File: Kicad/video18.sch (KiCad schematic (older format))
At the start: 18 parts, among them J201 DE15HD, U201 THS7316, U202 TPD7S019

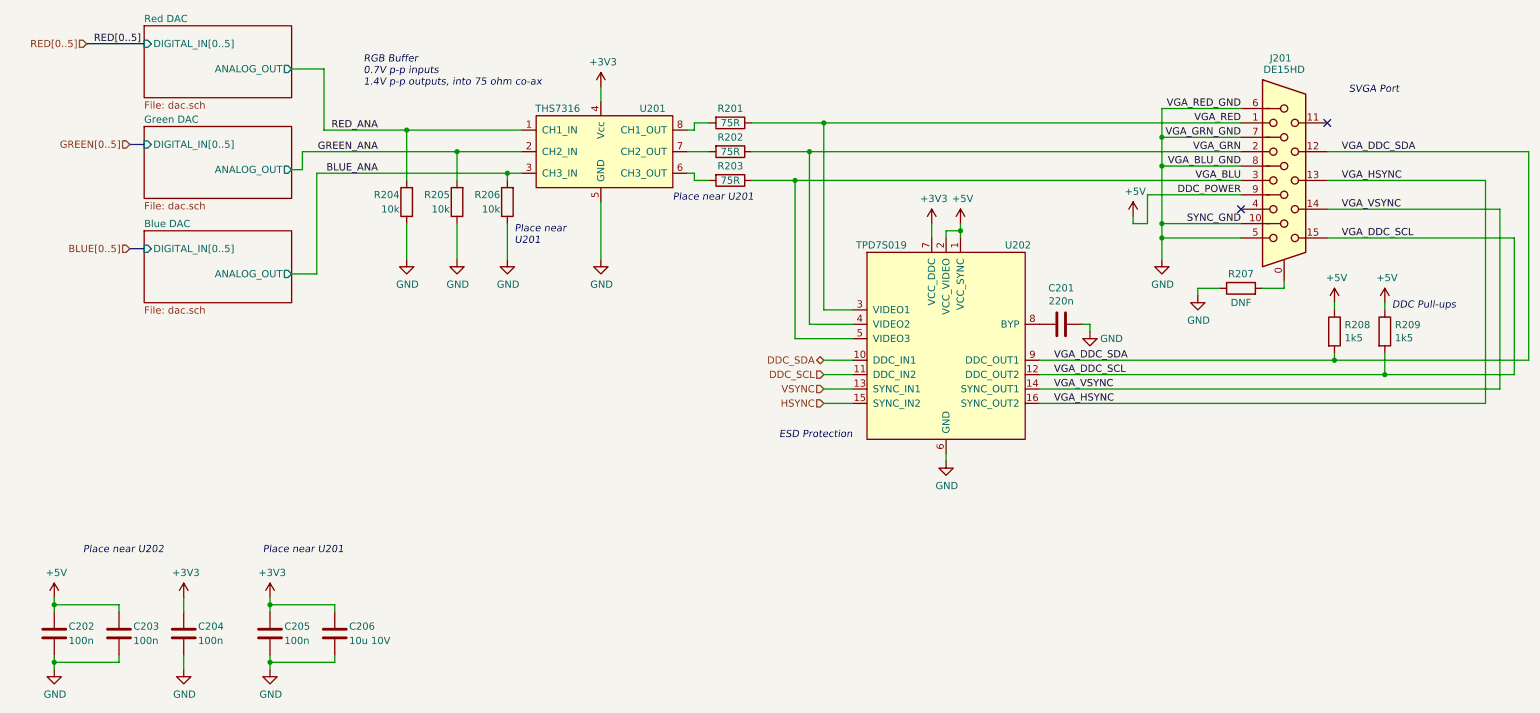
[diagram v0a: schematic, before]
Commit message: Added 12-bit video DAC.
Also had to change footprints to suit Kicad 5.1.9
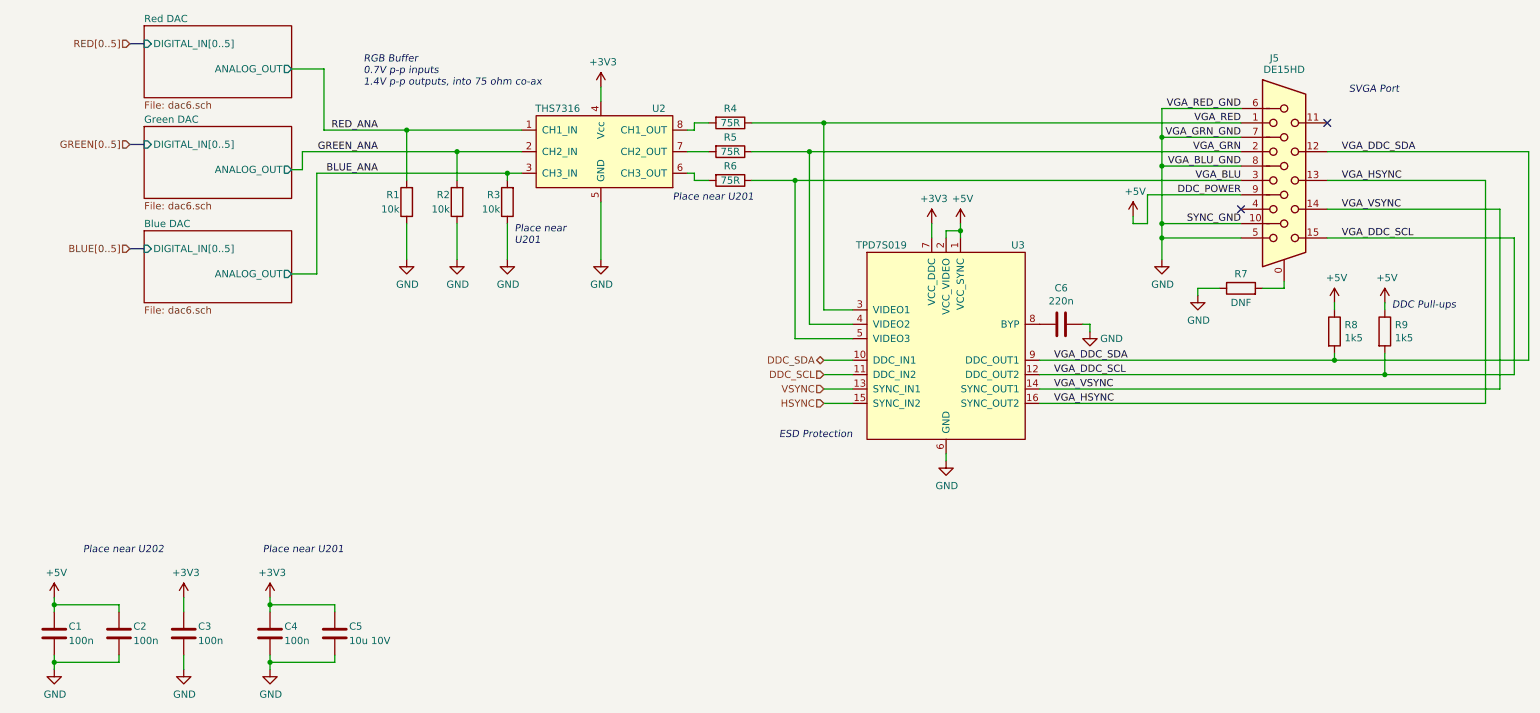
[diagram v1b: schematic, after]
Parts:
- removed C203, C205: 100n, Capacitor_SMD:C_0805_2012Metric_Pad1.15x1.40mm_HandSolder, symbol Device:C
- removed C206: 10u 10V, Capacitor_SMD:C_0805_2012Metric_Pad1.15x1.40mm_HandSolder, symbol Device:C
- removed R205, R206: 10k, Resistor_SMD:R_0805_2012Metric_Pad1.15x1.40mm_HandSolder, symbol Device:R
- removed R207: DNF, Resistor_SMD:R_0805_2012Metric_Pad1.15x1.40mm_HandSolder, symbol Device:R
- removed U201: THS7316, Package_SO:SOIC-8_3.9x4.9mm_P1.27mm, symbol Neotron-Common-Hardware:TPF133A
- removed U202: TPD7S019, Package_SO:SSOP-16_3.9x4.9mm_P0.635mm, symbol Neotron-Common-Hardware:TPD7S019
- added C2, C4: 100n, Capacitor_SMD:C_0805_2012Metric_Pad1.18x1.45mm_HandSolder, symbol Device:C
- added C5: 10u 10V, Capacitor_SMD:C_0805_2012Metric_Pad1.18x1.45mm_HandSolder, symbol Device:C
- added R2, R3: 10k, Resistor_SMD:R_0805_2012Metric_Pad1.20x1.40mm_HandSolder, symbol Device:R
- added R7: DNF, Resistor_SMD:R_0805_2012Metric_Pad1.20x1.40mm_HandSolder, symbol Device:R
- added U2: THS7316, Package_SO:SOIC-8_3.9x4.9mm_P1.27mm, symbol Neotron-Common-Hardware:TPF133A
- added U3: TPD7S019, Package_SO:SSOP-16_3.9x4.9mm_P0.635mm, symbol Neotron-Common-Hardware:TPD7S019
- C1: renamed from C202; footprint Capacitor_SMD:C_0805_2012Metric_Pad1.15x1.40mm_HandSolder -> Capacitor_SMD:C_0805_2012Metric_Pad1.18x1.45mm_HandSolder
- C3: renamed from C204; footprint Capacitor_SMD:C_0805_2012Metric_Pad1.15x1.40mm_HandSolder -> Capacitor_SMD:C_0805_2012Metric_Pad1.18x1.45mm_HandSolder
- C6: renamed from C201; footprint Capacitor_SMD:C_0805_2012Metric_Pad1.15x1.40mm_HandSolder -> Capacitor_SMD:C_0805_2012Metric_Pad1.18x1.45mm_HandSolder
- R1: renamed from R204; footprint Resistor_SMD:R_0805_2012Metric_Pad1.15x1.40mm_HandSolder -> Resistor_SMD:R_0805_2012Metric_Pad1.20x1.40mm_HandSolder
- R4: renamed from R201; footprint Resistor_SMD:R_0805_2012Metric_Pad1.15x1.40mm_HandSolder -> Resistor_SMD:R_0805_2012Metric_Pad1.20x1.40mm_HandSolder
- R5: renamed from R202; footprint Resistor_SMD:R_0805_2012Metric_Pad1.15x1.40mm_HandSolder -> Resistor_SMD:R_0805_2012Metric_Pad1.20x1.40mm_HandSolder
- R6: renamed from R203; footprint Resistor_SMD:R_0805_2012Metric_Pad1.15x1.40mm_HandSolder -> Resistor_SMD:R_0805_2012Metric_Pad1.20x1.40mm_HandSolder
- R8: renamed from R208; footprint Resistor_SMD:R_0805_2012Metric_Pad1.15x1.40mm_HandSolder -> Resistor_SMD:R_0805_2012Metric_Pad1.20x1.40mm_HandSolder
- R9: renamed from R209; footprint Resistor_SMD:R_0805_2012Metric_Pad1.15x1.40mm_HandSolder -> Resistor_SMD:R_0805_2012Metric_Pad1.20x1.40mm_HandSolder
- renumbered J201 to J5
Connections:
- net +3V3: now also C4.2, C5.1, U2.4 (Vcc), U3.7 (VCC_DDC)
- net +5V: now also C2.2, U3.1 (VCC_SYNC), U3.2 (VCC_VIDEO)
- net BLUE_ANA: now also R3.2, U2.3 (CH3_IN)
- net DDC_SCL: now also U3.11 (DDC_IN2)
- net DDC_SDA: now also U3.10 (DDC_IN1)
- net GND: now also C2.1, C4.1, C5.2, R2.1, R3.1, R7.1, U2.5 (GND), U3.6 (GND)
- net GREEN_ANA: now also R2.2, U2.2 (CH2_IN)
- net HSYNC: now also U3.15 (SYNC_IN2)
- net RED_ANA: now also U2.1 (CH1_IN)
- net VGA_BLU: now also U3.5 (VIDEO3)
- net VGA_DDC_SCL: now also U3.12 (DDC_OUT2)
- net VGA_DDC_SDA: now also U3.9 (DDC_OUT1)
- net VGA_GRN: now also U3.4 (VIDEO2)
- net VGA_HSYNC: now also U3.16 (SYNC_OUT2)
- net VGA_RED: now also U3.3 (VIDEO1)
- net VGA_VSYNC: now also U3.14 (SYNC_OUT1)
- net VSYNC: now also U3.13 (SYNC_IN1)
- net at J5.0: now also R7.2
- net at R4.2: now also U2.8 (CH1_OUT)
- net at R5.2: now also U2.7 (CH2_OUT)
- net at R6.2: now also U2.6 (CH3_OUT)
- net at C6.2: now also U3.8 (BYP)

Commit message: Add 4-bit Video DAC, and re-wire BMC.
Now the BMC is an SPI device, and has a four-wire UART.
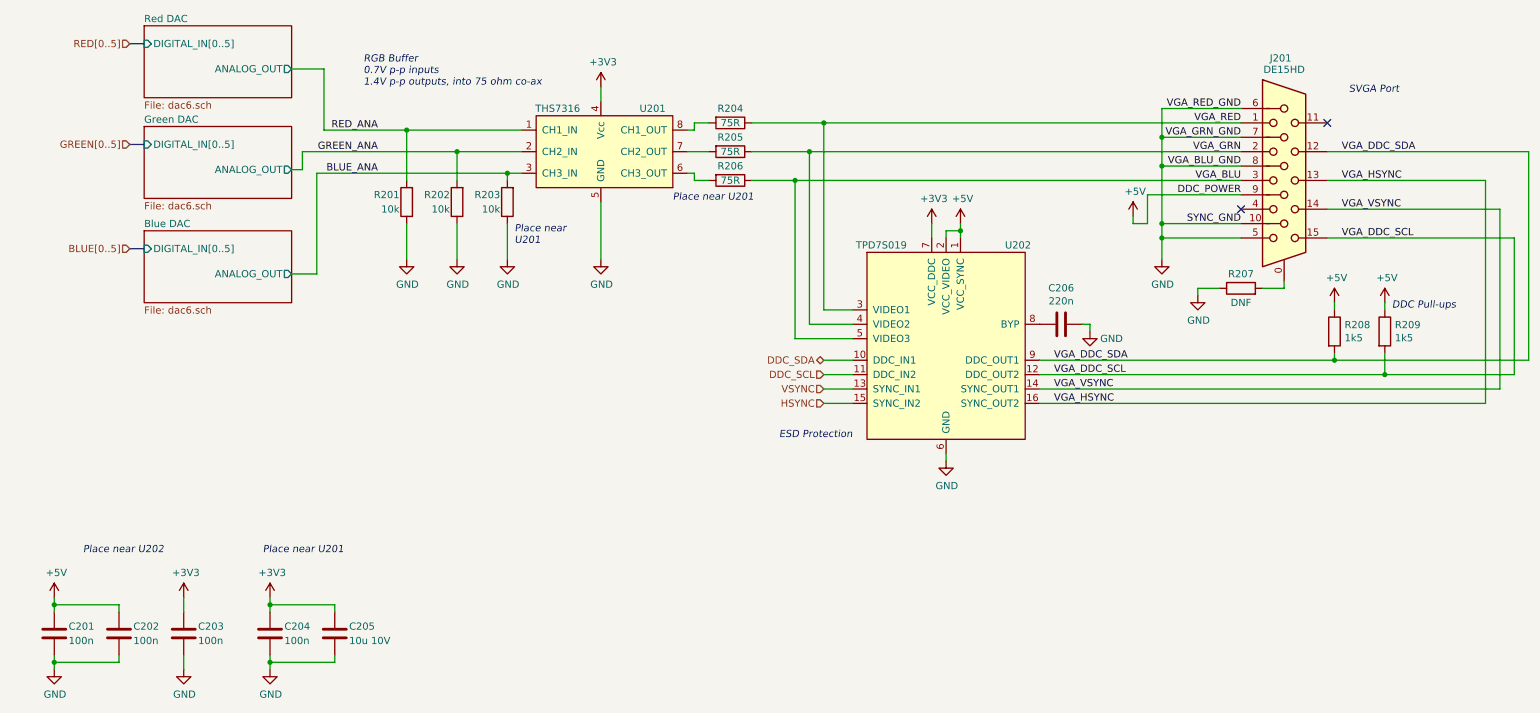
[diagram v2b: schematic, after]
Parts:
- renumbered C1 to C201, C2 to C202, C3 to C203, C4 to C204, C5 to C205, C6 to C206, J5 to J201, R1 to R201, R2 to R202, R3 to R203, R4 to R204, R5 to R205, R6 to R206, R7 to R207, R8 to R208, R9 to R209, U2 to U201, U3 to U202

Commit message: Tidy up part nos and swapped I2C/UART on BMC.
Mark all resistors as 1% if not specified.
Added some Mouser part numbers.
BMC can now be programmed over UART.
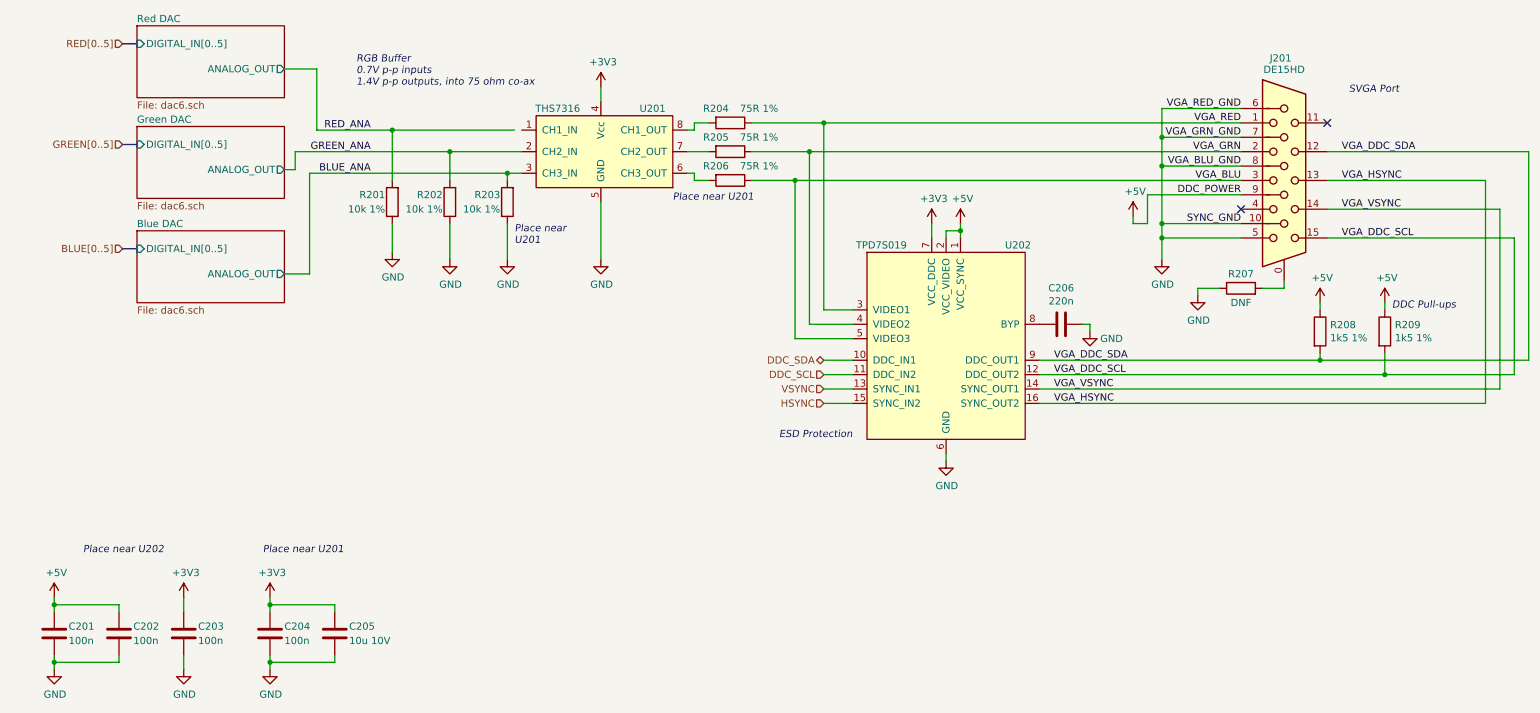
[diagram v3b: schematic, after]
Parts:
- C201, C202, C203, C204: Mouser (none) -> 594-K104K15X7RF5TL2
- J201: Mouser (none) -> 649-ICD15S13E4GV00LF
- R201, R202, R203: value 10k -> 10k 1%
- R204, R205, R206: value 75R -> 75R 1%
- R208, R209: value 1k5 -> 1k5 1%
- U201: Mouser (none) -> 595-THS7316DR
- U202: Mouser (none) -> 595-TPD7S019-15DBQR
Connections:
- net RED_ANA: no longer U201.1 (CH1_IN)
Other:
- moved on the sheet: R201, R202, R208

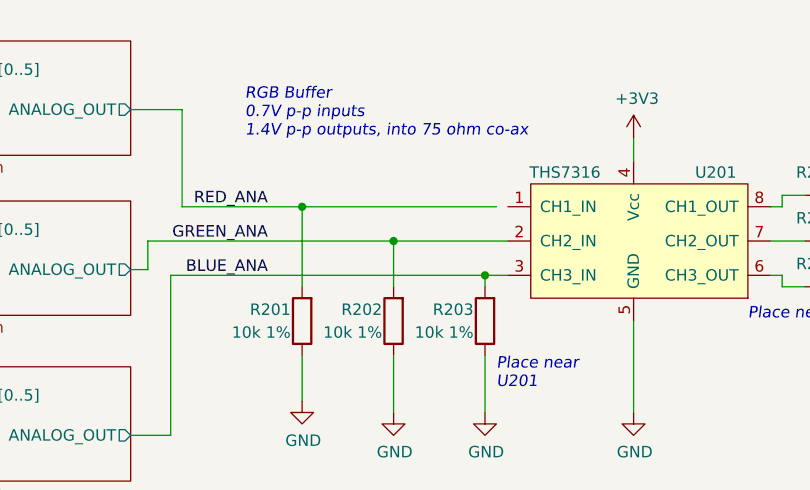
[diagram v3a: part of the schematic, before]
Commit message: Changes to BMC
* Swapped BUTTON_PWR and SYS_RESET to avoid DRC issue
* Split PSU and BMC into two separate sheets
* Swapped some pins on the STM32 to make it compatible with more
alternatives
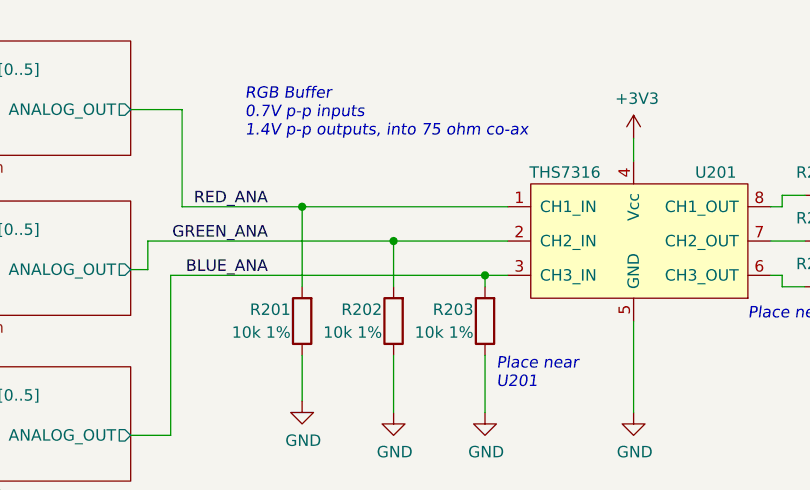
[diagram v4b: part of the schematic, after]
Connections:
- net RED_ANA: now also U201.1 (CH1_IN)
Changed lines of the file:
@@
 $Descr A4 11693 8268
 encoding utf-8
-Sheet 2 16
+Sheet 2 17
 Title "Neotron Common Hardware - Video Output"
 Date "2021-04-02"
@@
 	3150 4000 3150 3650
 Connection ~ 3150 3650
-Wire Wire Line
-	3150 3650 4000 3650
 $Comp
 L Neotron-Common-Hardware:TPD7S019 U202
@@
 Wire Wire Line
 	9600 5250 11050 5250
+Wire Wire Line
+	3150 3650 4050 3650
 $EndSCHEMATC
